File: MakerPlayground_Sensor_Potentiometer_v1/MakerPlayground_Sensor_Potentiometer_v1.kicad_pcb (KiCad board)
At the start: 2 copper layers, 30.4 x 19.9 mm, 5 parts, among them J1 Conn_01x04

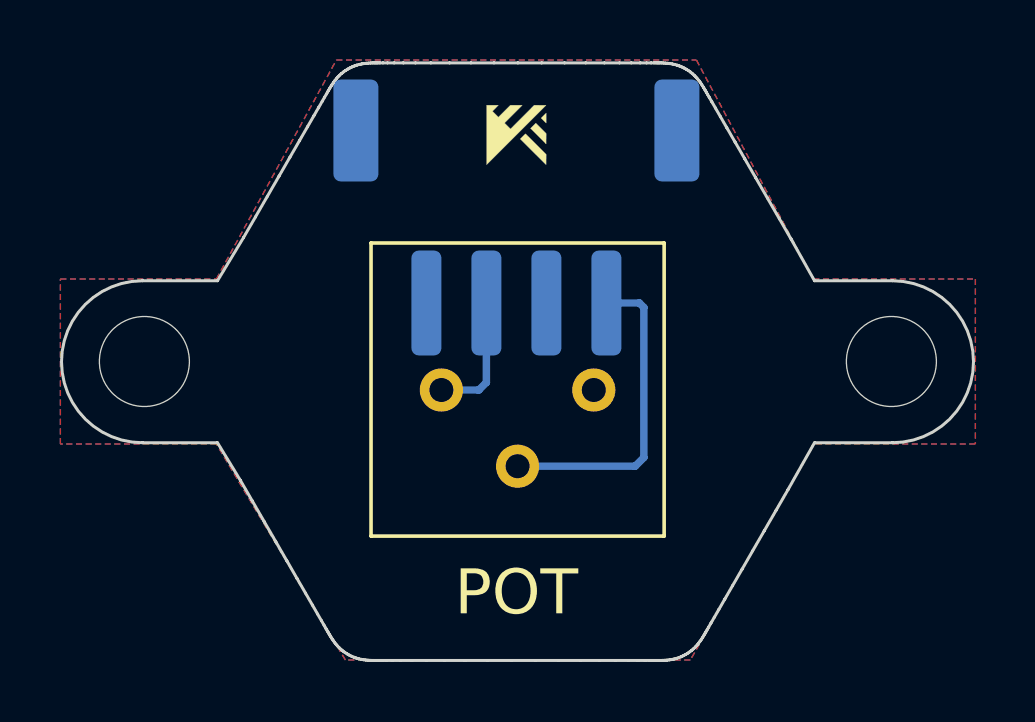
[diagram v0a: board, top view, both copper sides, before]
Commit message: Single HEX design; Lock mounting hole footprint & review mounting hole position.
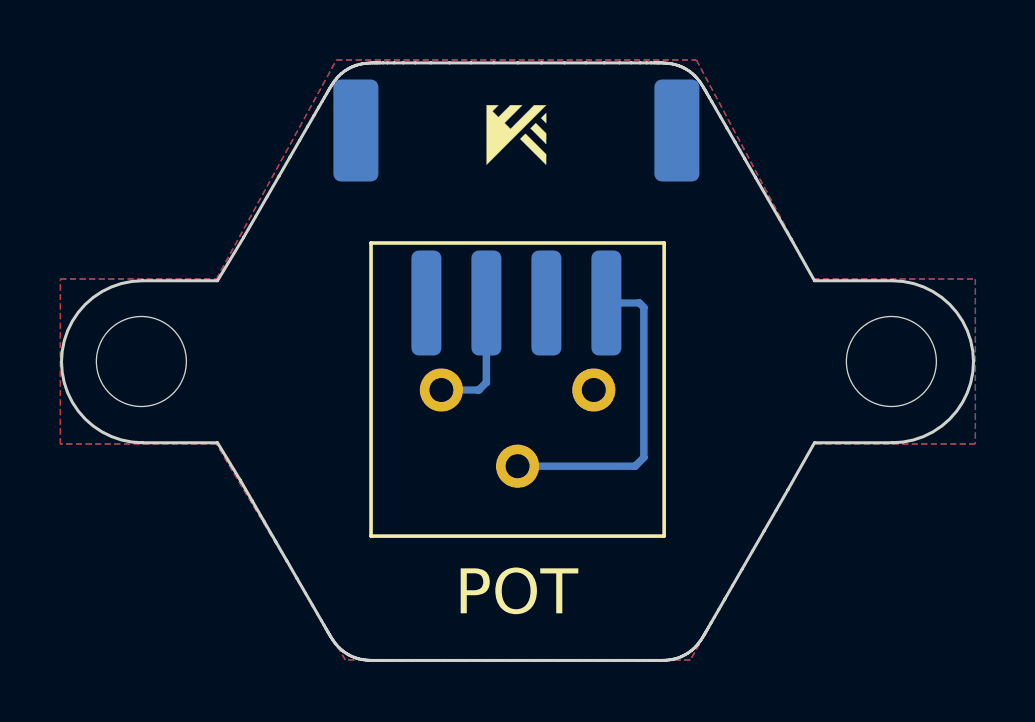
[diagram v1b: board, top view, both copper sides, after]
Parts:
- moved REF** 0.10 mm to (134.0, 100.0)
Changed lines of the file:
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@@
     (add_net "Net-(J1-Pad3)")
   )
-  (module MountingHole:MountingHole_3mm (layer F.Cu)
+  (module MountingHole:MountingHole_3mm locked (layer F.Cu)
     (at 159 100.05)
     (descr "Mounting Hole 3mm, no annular")
@@
       (xy 0.199355 -0.596628) (xy 0.593328 -0.992663) (xy 0.790777 -0.991434)) (layer F.SilkS) (width 0.01))
   )
-  (module MountingHole:MountingHole_3mm (layer F.Cu)
-    (at 134.1 100.05)
+  (module MountingHole:MountingHole_3mm locked (layer F.Cu)
+    (at 134 100.05)
     (descr "Mounting Hole 3mm, no annular")
     (tags "mounting hole 3mm no annular")

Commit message: Complete design.
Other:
- board text added: "v1.0"
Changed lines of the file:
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@@
   (general
     (thickness 1.6)
-    (drawings 223)
+    (drawings 224)
     (tracks 8)
     (zones 0)
@@
     (46 B.CrtYd user)
     (47 F.CrtYd user)
-    (48 B.Fab user)
-    (49 F.Fab user)
+    (48 B.Fab user hide)
+    (49 F.Fab user hide)
   )
   (setup
@@
     (pad 1 np_thru_hole circle (at 0 0) (size 3 3) (drill 3) (layers *.Cu *.Mask))
   )
+  (gr_text v1.0 (at 147.75 109.25) (layer F.SilkS)
+    (effects (font (size 0.5 0.5) (thickness 0.1)))
+  )
   (gr_arc (start 159.037 100.0583) (end 159.037 102.7583) (angle -180) (layer Edge.Cuts) (width 0.1))
